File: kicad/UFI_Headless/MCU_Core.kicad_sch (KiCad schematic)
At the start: 80 parts, among them J12 FRONT, J20 GUARD, J21 LA, J4 SWD, J5 DBG_UART, SW1 RESET, SW2 BOOT, SW3 BTN_A, SW4 BTN_B, U11 APS6404L-3SQR-SN, U15 CSNP32GCR01-AOW, U5 STM32H723ZGT6, Y1 25MHz CL=12pF

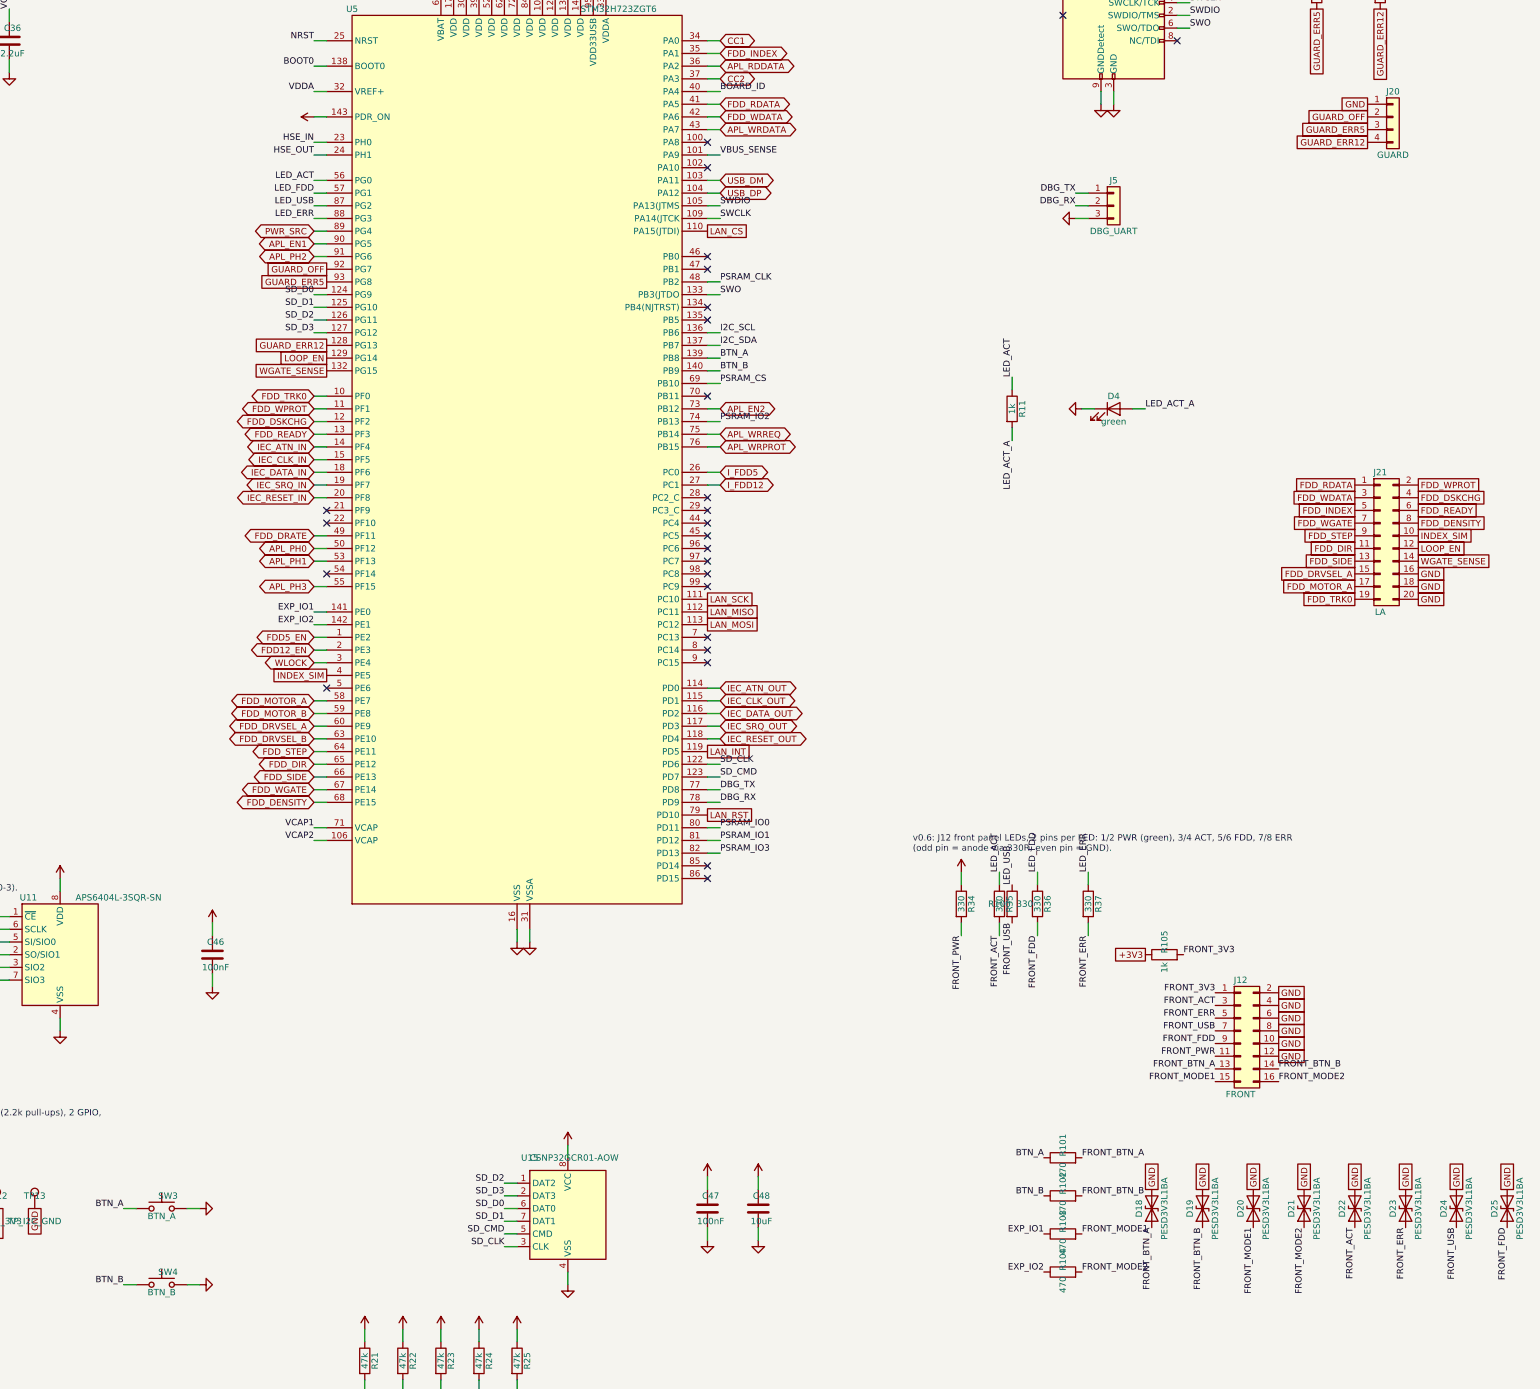
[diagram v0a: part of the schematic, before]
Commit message: KiCad v0.7 rework, stage A9a (owner review of 2026-10-24, protection items before the B3 re-layout): J17 PSU-IN and J3 drive power become keyed JST XH B4B-XH-A (LCSC C144395, 3 A, same pin order 1 +5V 2/3 GND 4 +12V) because a reversed 2.54-mm header would have put 12 V on U19 (6 V max) or on the drive's 5 V input - adapter cables Berg <-> XH described in kicad/UFI_Headless/docs/Inbetriebnahme.md; D27 SS54 (C16103) from J17 pin 4 (new local net +12V_PSU) to +12V as a diode-OR with D2, so the jack and the C64 PSU may be plugged at once; U24 USBLC6-2SC6 (C7519, VRWM 5.25 V) on CC1/CC2 next to J1 (the USBLC6 U1 only covers D+/D-); R125-R127 220 R (C22962) in series on the GUARD cable, cable side GUARD_OFF_J/GUARD_ERR5_J/GUARD_ERR12_J, MCU side unchanged with the 10k pull-ups; R26/R29 0.1 R -> 50 mR 1 % (TA-I RLM12FTCMR050 C912768, alternative Panasonic ERJ8CWFR050V C713437, stock to be checked in stage C) and F2 1206 -> 1812 like F3 (C20999) to cut the series resistance of the 5 V drive chain; SW3/SW4 (DNP buttons A/B) deleted from the schematic incl. their labels and GND symbols, buttons stay on the front header J12 pin 13/14. Firmware in the same commit: ufi_board.c scales the INA180 reading by board revision (v1.0 50 mR = 1 mV/mA, v0.x 0.1 R = 2 mV/mA via ufi_board_rev()), comments in board.h; protocol doc BOARD_STATUS mA fields note the scale. ERC over the whole project 0 errors / 0 warnings (build/erc.rpt refreshed, it had been from 7.10. without the LAN sheet); ARM build 0 warnings, AXI free 36688 B unchanged; offline gate: all 23 check groups green, the final pytest step of the owner's check_all.py reports "No module named pytest" in this environment (not related to this change). fertigung/: the v0.x Gerber/BOM/CPL/zip of 7.10. removed (README stub explains), nothing may be ordered before stage C. PLAN.md: row A9 with the owner's ten-point definition (A9a done; A9b write-protect default-on + INDEX on TIM2_CH4 + pin map, A9c soft start + RTC open), B3 row; kicad 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
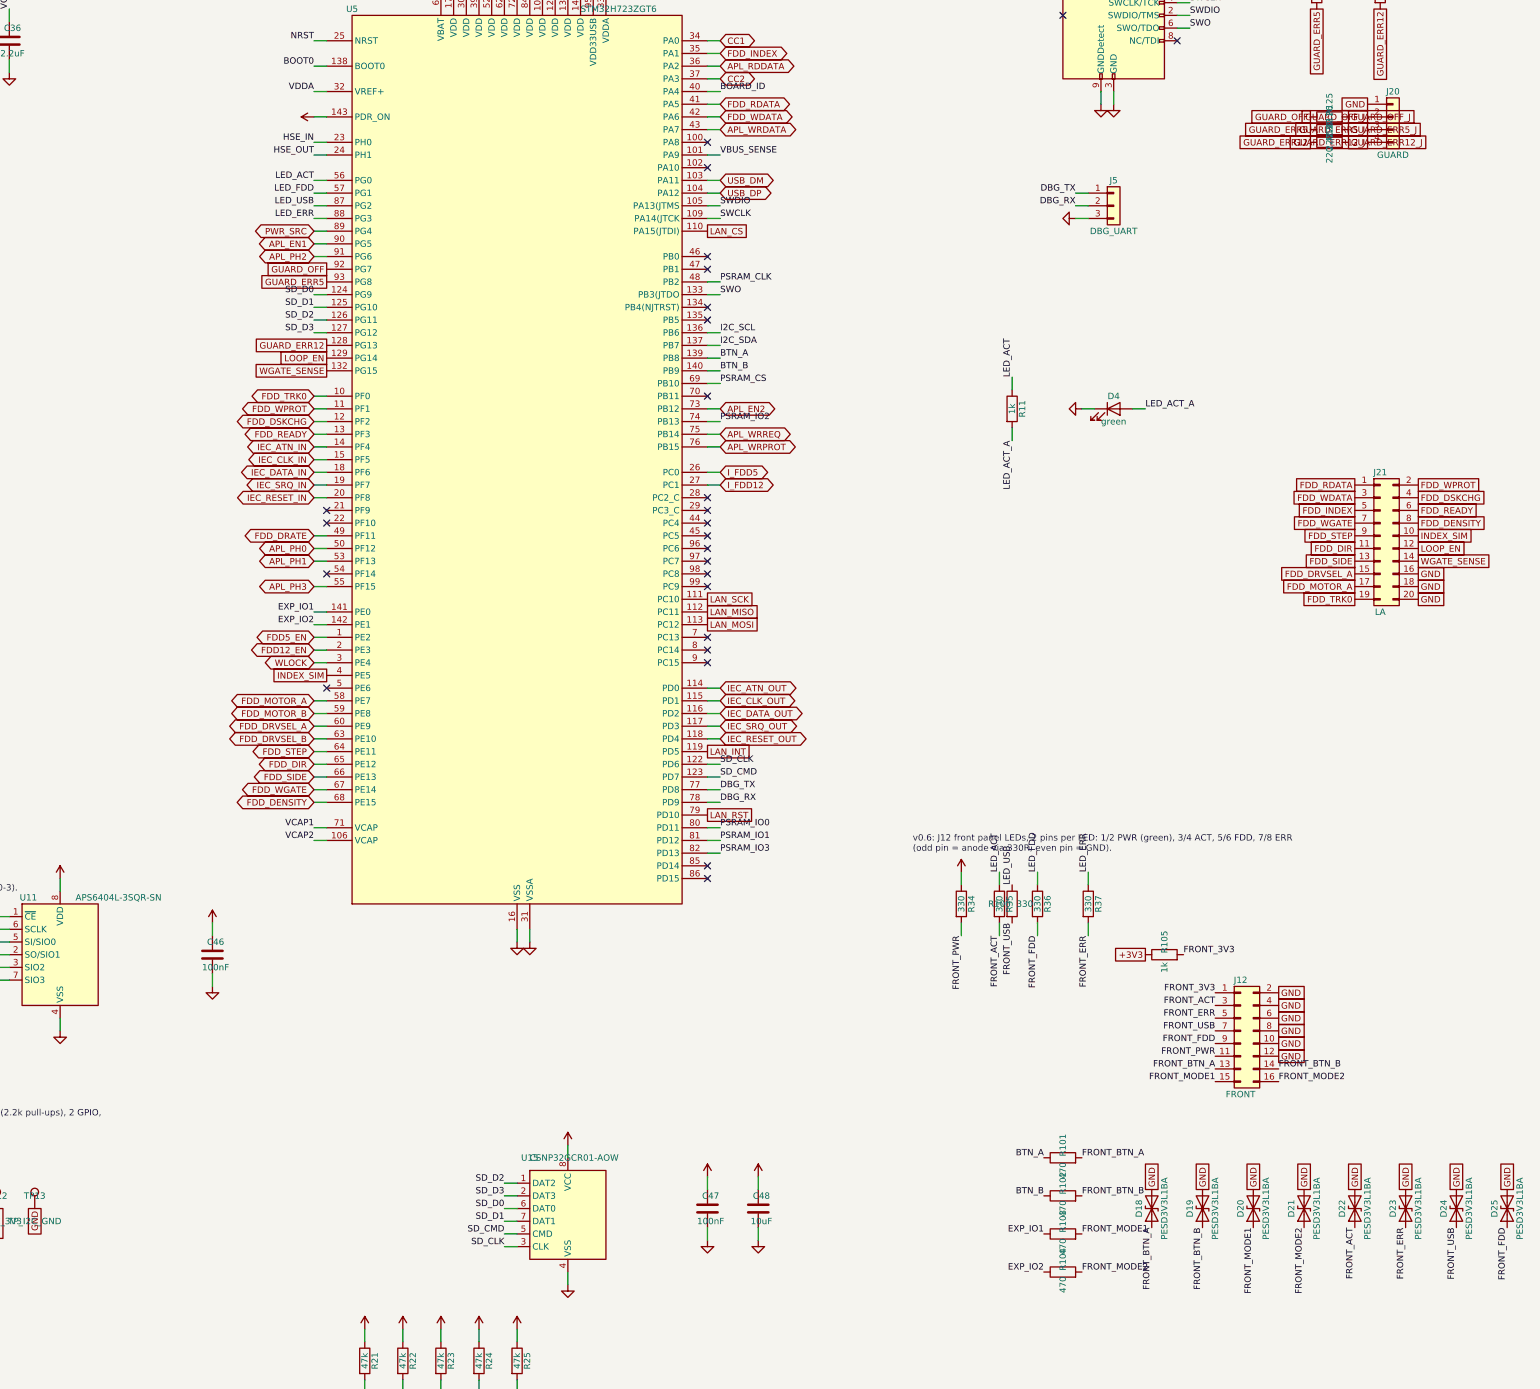
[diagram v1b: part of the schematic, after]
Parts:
- removed SW3: BTN_A, Button_Switch_SMD:SW_SPST_TL3342, symbol Switch:SW_Push
- removed SW4: BTN_B, Button_Switch_SMD:SW_SPST_TL3342, symbol Switch:SW_Push
- added R125, R126, R127: 220, Resistor_SMD:R_0603_1608Metric, symbol Device:R
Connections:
- net GUARD_ERR12: now also R127.1; no longer J20.4 (Pin_4)
- net GUARD_ERR5: now also R126.1; no longer J20.3 (Pin_3)
- net GUARD_OFF: now also R125.1; no longer J20.2 (Pin_2)
- new net GUARD_ERR12_J: J20.4 (Pin_4), R127.2
- new net GUARD_ERR5_J: J20.3 (Pin_3), R126.2
- new net GUARD_OFF_J: J20.2 (Pin_2), R125.2

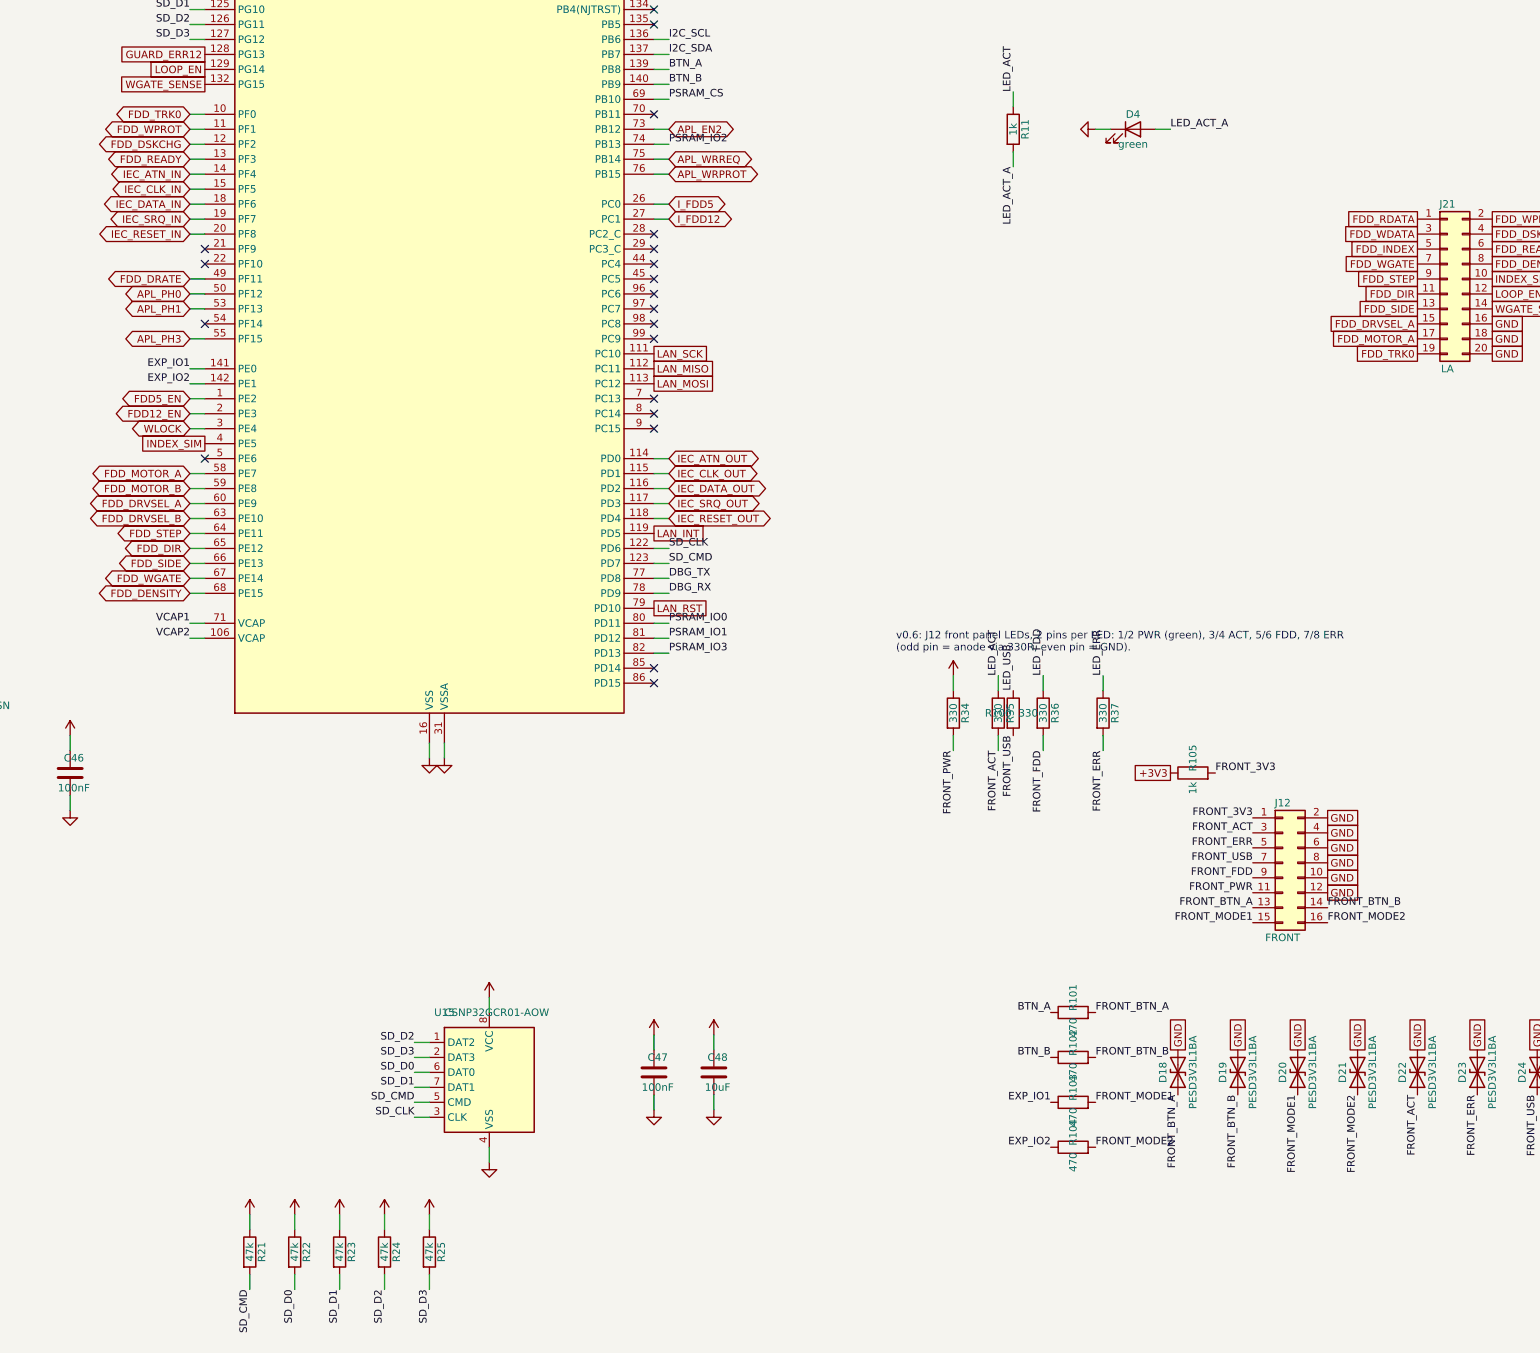
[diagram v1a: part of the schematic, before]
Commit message: KiCad v0.7 rework, stage A9b (owner definition of 2026-10-24): write protection is on by default and INDEX also reaches TIM2_CH4 - Flux_Interface: R33 becomes a 10k pull-up from WLOCK_HW to +3V3 (C25804; was 100k to GND), the solder jumper JP4 is gone, U14 74LVC1G32 -> 74LVC1G332 3-input OR (TI SN74LVC1G332DCKR C2865081, SC-70-6; alternative Nexperia 74LVC1G332GW C548342) with FDD_WGATE, WLOCK_HW and WLOCK_FW as inputs and FDD_WGATE_G as output, R131 100k pull-up on WLOCK_FW so the gate is closed through reset and boot; MCU_Core: U5 PE4 = WLOCK_FW (output), PE6 = WREN_SENSE through R130 470 R from WLOCK_HW, PB11 = FDD_INDEX (TIM2_CH4, AF1 verified against the STM32H723ZG pin database: PB11 TIM2 CH4 AF1, PE4/PE6 plain GPIO, PC14/PC15 OSC32), no-connect flags on PE6/PB11 removed; front header J12 pin 12 = WLOCK_HW (switch SCHREIBEN to GND = write enabled, cable off = locked), pin 10 = FRONT_WRLED (+3V3 through R128 1k, LED anode; LED cathode on pin 12 lights "write enabled"), D28/D29 PESD3V3L1BA on both, even pins 2-8 stay GND; J12 note updated. Firmware in the same commit: board.h/board_headless.c PE4 driven high before it becomes an output (no low glitch into the OR gate), PE6 input, PB11 AF1 input (the capture code keeps using CH2 on PA1 - CH4 is wired for the pulse-width measurement later), ufi_board.c ufi_board_jumper_locked() reads PE6 on board_rev >= 10 and PE4 on v0.x, new ufi_board_write_enable(on) drives WLOCK_FW low only while a write runs (on v0.x it restores PE4 as the jumper input once), ufi_write.c calls it after the lock checks and in write_finish (two hunks staged from the owner's working copy); protocol doc: board_status flags bit 0 explained for v1.0. ERC over the whole project 0 errors / 0 warnings (build/erc.rpt); ARM build and offline gate as reported in the stage log. PLAN.md A9 row (A9b done, A9c soft start + RTC open), kicad README (A9b row, GPIO table PE4/PE6/PB11). The PCB follows in B3.
Claude-Session: https://claude.ai/code/session_014Mdzr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
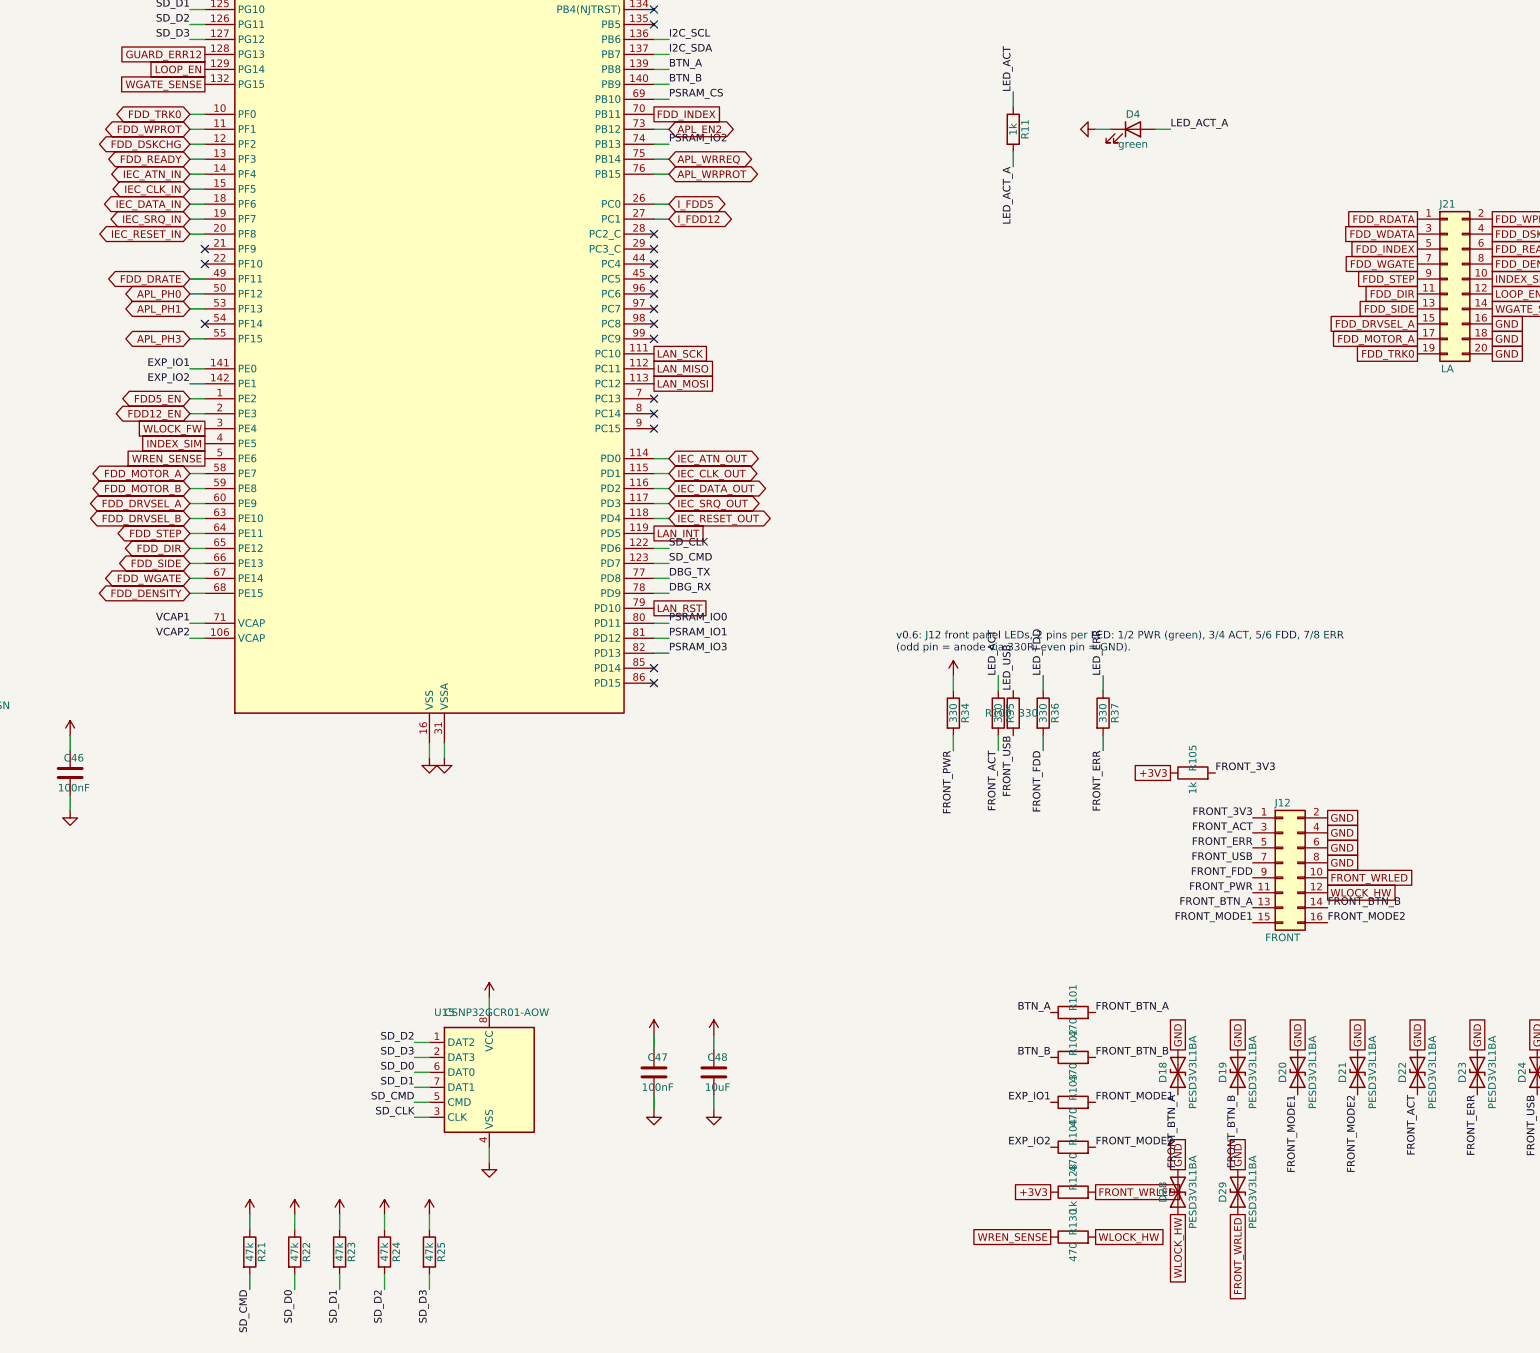
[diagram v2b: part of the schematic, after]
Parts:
- added D28, D29: PESD3V3L1BA, Diode_SMD:D_SOD-323, symbol Device:D_TVS
- added R128: 1k, Resistor_SMD:R_0603_1608Metric, symbol Device:R
- added R130: 470, Resistor_SMD:R_0603_1608Metric, symbol Device:R
- J12: Note front panel, keyed 2x8: 1 +3V3, 3 ACT, 5 ERR, 7 USB, 9 FDD,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 -> front panel, keyed 2x8: 1 +3V3 (R105), 3 ACT, 5 ERR, 7 USB,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
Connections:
- net +3V3: now also R128.1
- net FDD_INDEX: now also U5.70 (PB11)
- net GND: now also D28.2 (A2), D29.2 (A2); no longer J12.10 (Pin_10), J12.12 (Pin_12)
- net WREN_SENSE: now reaches U5.5 (PE6)
- net WREN_SENSE: now also R130.1
- net WLOCK renamed WLOCK_FW
- new net FRONT_WRLED: D29.1 (A1), J12.10 (Pin_10), R128.2
- new net WLOCK_HW: D28.1 (A1), J12.12 (Pin_12), R130.2
- no-connect marks 26 -> 24
